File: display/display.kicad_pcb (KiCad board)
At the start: 2 copper layers, 80 x 20 mm, 48 parts, among them P1 CONN_14

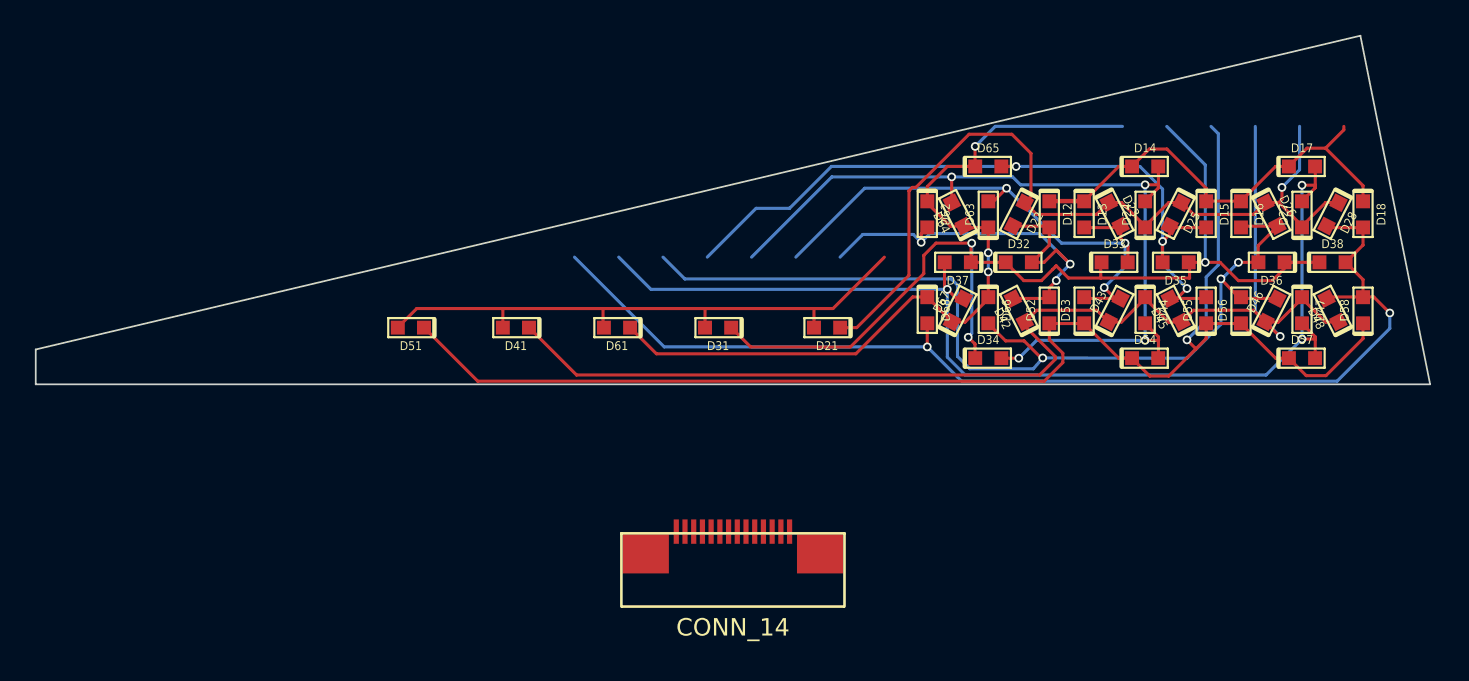
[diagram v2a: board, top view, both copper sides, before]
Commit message: Remove board contours.
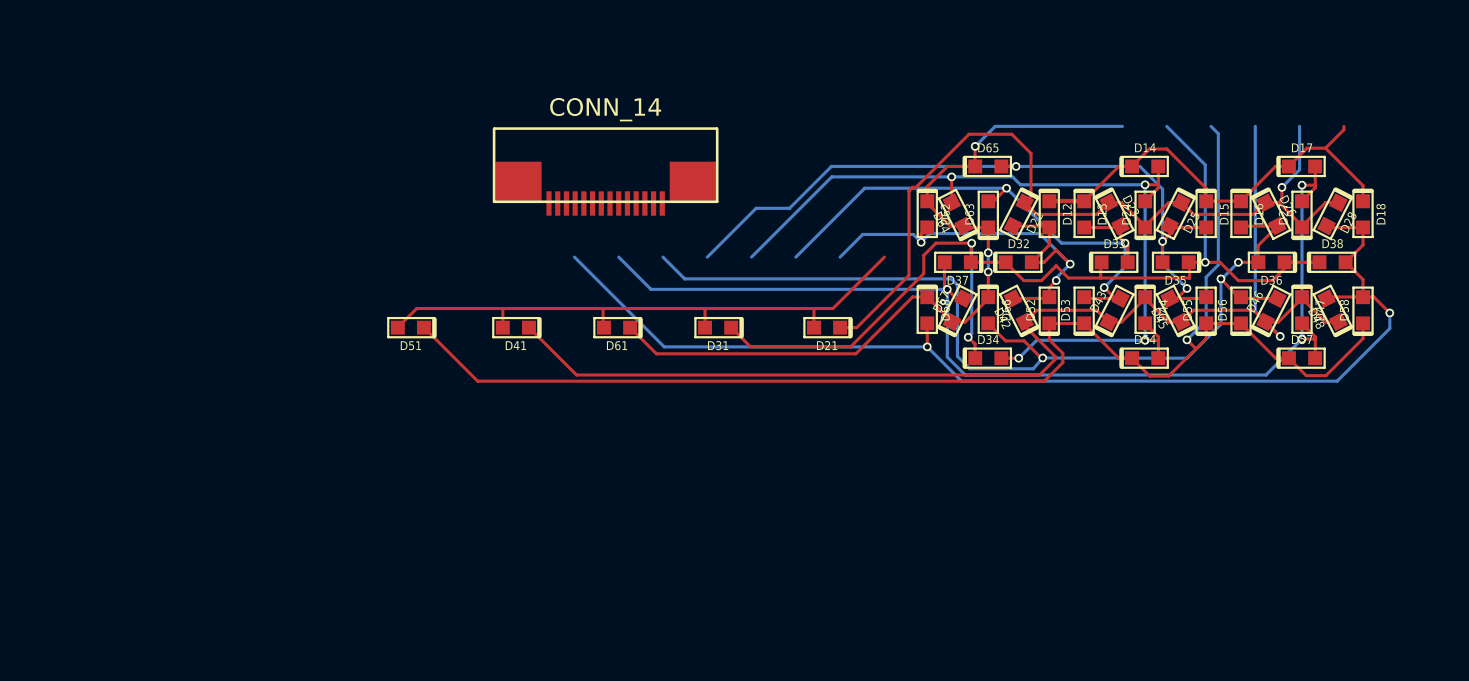
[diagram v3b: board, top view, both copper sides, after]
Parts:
- moved P1 28.4 mm to (135.4, 94.4), turned to 180 degrees
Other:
- board outline removed
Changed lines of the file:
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@@
     (area 102.642669 89.033349 182.741571 109.132371)
     (thickness 1.6002)
-    (drawings 5)
+    (drawings 1)
     (tracks 356)
     (zones 0)
@@
   )
   (module SFV14R-2STE1HLF (layer Front)
-    (at 142.69212 121.832371)
-    (fp_text reference P1 (at 0 -6.3) (layer F.SilkS) hide
+    (at 135.39 94.41 180)
+    (fp_text reference P1 (at 0 -6.3 180) (layer F.SilkS) hide
       (effects (font (size 1 1) (thickness 0.15)))
     )
-    (fp_text value CONN_14 (at 0 1.2) (layer F.SilkS)
+    (fp_text value CONN_14 (at 0 1.2 180) (layer F.SilkS)
       (effects (font (size 1 1) (thickness 0.15)))
     )
@@
     (fp_line (start -6.4 -4.2) (end 6.4 -4.2) (layer F.SilkS) (width 0.15))
     (fp_line (start -6.35 0) (end 6.35 0) (layer F.SilkS) (width 0.15))
-    (pad 4 smd rect (at -1.75 -4.3) (size 0.3 1.4)
+    (pad 4 smd rect (at -1.75 -4.3 180) (size 0.3 1.4)
       (layers Front F.Paste F.Mask)
       (net 12 /ROW4)
     )
-    (pad 5 smd rect (at -1.25 -4.3) (size 0.3 1.4)
+    (pad 5 smd rect (at -1.25 -4.3 180) (size 0.3 1.4)
       (layers Front F.Paste F.Mask)
       (net 13 /ROW5)
     )
-    (pad 6 smd rect (at -0.75 -4.3) (size 0.3 1.4)
+    (pad 6 smd rect (at -0.75 -4.3 180) (size 0.3 1.4)
       (layers Front F.Paste F.Mask)
       (net 14 /ROW6)
     )
-    (pad 7 smd rect (at -0.25 -4.3) (size 0.3 1.4)
+    (pad 7 smd rect (at -0.25 -4.3 180) (size 0.3 1.4)
       (layers Front F.Paste F.Mask)
       (net 1 /COL1)
     )
-    (pad 8 smd rect (at 0.25 -4.3) (size 0.3 1.4)
+    (pad 8 smd rect (at 0.25 -4.3 180) (size 0.3 1.4)
       (layers Front F.Paste F.Mask)
       (net 2 /COL2)
     )
-    (pad 9 smd rect (at 0.75 -4.3) (size 0.3 1.4)
+    (pad 9 smd rect (at 0.75 -4.3 180) (size 0.3 1.4)
       (layers Front F.Paste F.Mask)
       (net 3 /COL3)
     )
-    (pad 10 smd rect (at 1.25 -4.3) (size 0.3 1.4)
+    (pad 10 smd rect (at 1.25 -4.3 180) (size 0.3 1.4)
       (layers Front F.Paste F.Mask)
       (net 4 /COL4)
     )
-    (pad 11 smd rect (at 1.75 -4.3) (size 0.3 1.4)
+    (pad 11 smd rect (at 1.75 -4.3 180) (size 0.3 1.4)
       (layers Front F.Paste F.Mask)
       (net 5 /COL5)
     )
-    (pad 12 smd rect (at 2.25 -4.3) (size 0.3 1.4)
+    (pad 12 smd rect (at 2.25 -4.3 180) (size 0.3 1.4)
       (layers Front F.Paste F.Mask)
       (net 6 /COL6)
     )
-    (pad 3 smd rect (at -2.25 -4.3) (size 0.3 1.4)
+    (pad 3 smd rect (at -2.25 -4.3 180) (size 0.3 1.4)
       (layers Front F.Paste F.Mask)
       (net 11 /ROW3)
     )
-    (pad 13 smd rect (at 2.75 -4.3) (size 0.3 1.4)
+    (pad 13 smd rect (at 2.75 -4.3 180) (size 0.3 1.4)
       (layers Front F.Paste F.Mask)
       (net 7 /COL7)
     )
-    (pad 14 smd rect (at 3.25 -4.3) (size 0.3 1.4)
+    (pad 14 smd rect (at 3.25 -4.3 180) (size 0.3 1.4)
       (layers Front F.Paste F.Mask)
       (net 8 /COL8)
     )
-    (pad 2 smd rect (at -2.75 -4.3) (size 0.3 1.4)
+    (pad 2 smd rect (at -2.75 -4.3 180) (size 0.3 1.4)
       (layers Front F.Paste F.Mask)
       (net 10 /ROW2)
     )
-    (pad 1 smd rect (at -3.25 -4.3) (size 0.3 1.4)
+    (pad 1 smd rect (at -3.25 -4.3 180) (size 0.3 1.4)
       (layers Front F.Paste F.Mask)
       (net 9 /ROW1)
     )
-    (pad "" smd rect (at -5 -3.05) (size 2.65 2.3)
-      (layers Front F.Paste F.Mask)
-    )
-    (pad "" smd rect (at 5 -3.05) (size 2.65 2.3)
+    (pad "" smd rect (at -5 -3.05 180) (size 2.65 2.3)
+      (layers Front F.Paste F.Mask)
+    )
+    (pad "" smd rect (at 5 -3.05 180) (size 2.65 2.3)
       (layers Front F.Paste F.Mask)
     )
@@
     (effects (font (size 1.5 1.5) (thickness 0.3)) (justify left))
   )
-  (gr_line (start 102.6922 107.08386) (end 102.6922 109.08284) (angle 90) (layer Edge.Cuts) (width 0.09906))
-  (gr_line (start 178.69154 89.08288) (end 102.6922 107.08386) (angle 90) (layer Edge.Cuts) (width 0.09906))
-  (gr_line (start 182.69204 109.08284) (end 178.69154 89.08288) (angle 90) (layer Edge.Cuts) (width 0.09906))
-  (gr_line (start 102.6922 109.08284) (end 182.69204 109.08284) (angle 90) (layer Edge.Cuts) (width 0.09906))
   (segment (start 147.33016 105.83164) (end 147.34286 105.81894) (width 0.1778) (layer Front) (net 0))
   (segment (start 147.34286 105.81894) (end 147.34286 104.73436) (width 0.1778) (layer Front) (net 0))

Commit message: Precision-place the new contour.
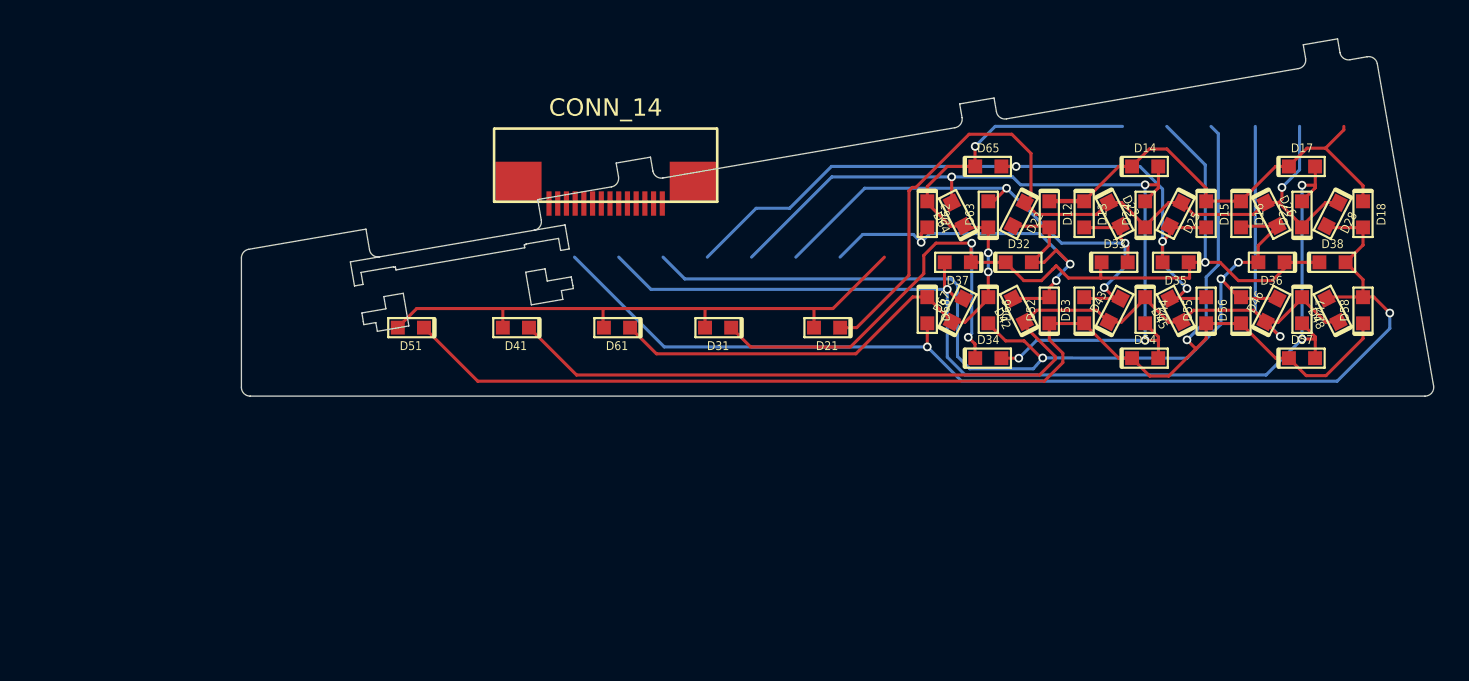
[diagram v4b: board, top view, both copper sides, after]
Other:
- board outline added: 68.4 x 20.5 mm
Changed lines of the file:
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@@
     (links 0)
     (no_connects 0)
-    (area 102.642669 89.033349 182.741571 109.132371)
+    (area 102.35 82.69 182.89528 109.763421)
     (thickness 1.6002)
-    (drawings 1)
+    (drawings 70)
     (tracks 356)
     (zones 0)
@@
     (effects (font (size 1.5 1.5) (thickness 0.3)) (justify left))
   )
+  (gr_line (start 120.742674 102.058041) (end 122.41886 101.769482) (angle 90) (layer Edge.Cuts) (width 0.01))
+  (gr_line (start 123.330283 102.353314) (end 123.231734 102.370282) (angle 90) (layer Edge.Cuts) (width 0.01))
+  (gr_line (start 123.35913 102.520856) (end 123.330283 102.353314) (angle 90) (layer Edge.Cuts) (width 0.01))
+  (gr_line (start 130.750395 101.248418) (end 123.35913 102.520856) (angle 90) (layer Edge.Cuts) (width 0.01))
+  (gr_line (start 130.721556 101.080884) (end 130.750395 101.248418) (angle 90) (layer Edge.Cuts) (width 0.01))
+  (gr_line (start 130.820105 101.063924) (end 130.721556 101.080884) (angle 90) (layer Edge.Cuts) (width 0.01))
+  (gr_line (start 130.815016 101.034352) (end 130.820105 101.063924) (angle 90) (layer Edge.Cuts) (width 0.01))
+  (gr_line (start 132.687476 100.712002) (end 130.815016 101.034352) (angle 90) (layer Edge.Cuts) (width 0.01))
+  (gr_line (start 132.806235 101.40186) (end 132.687476 100.712002) (angle 90) (layer Edge.Cuts) (width 0.01))
+  (gr_line (start 133.298987 101.317029) (end 132.806235 101.40186) (angle 90) (layer Edge.Cuts) (width 0.01))
+  (gr_line (start 133.061461 99.937321) (end 133.298987 101.317029) (angle 90) (layer Edge.Cuts) (width 0.01))
+  (gr_line (start 131.28839 100.242566) (end 133.061461 99.937321) (angle 90) (layer Edge.Cuts) (width 0.01))
+  (gr_line (start 120.9802 103.437749) (end 120.742674 102.058041) (angle 90) (layer Edge.Cuts) (width 0.01))
+  (gr_line (start 121.472945 103.352917) (end 120.9802 103.437749) (angle 90) (layer Edge.Cuts) (width 0.01))
+  (gr_line (start 121.354186 102.663068) (end 121.472945 103.352917) (angle 90) (layer Edge.Cuts) (width 0.01))
+  (gr_line (start 123.226645 102.340718) (end 121.354186 102.663068) (angle 90) (layer Edge.Cuts) (width 0.01))
+  (gr_line (start 123.231734 102.370282) (end 123.226645 102.340718) (angle 90) (layer Edge.Cuts) (width 0.01))
+  (gr_line (start 122.41886 101.769482) (end 131.28839 100.242566) (angle 90) (layer Edge.Cuts) (width 0.01))
+  (gr_line (start 130.803343 102.649754) (end 131.916968 102.458043) (angle 90) (layer Edge.Cuts) (width 0.01))
+  (gr_line (start 131.125693 104.522206) (end 130.803343 102.649754) (angle 90) (layer Edge.Cuts) (width 0.01))
+  (gr_line (start 132.934653 104.210789) (end 131.125693 104.522206) (angle 90) (layer Edge.Cuts) (width 0.01))
+  (gr_line (start 132.848128 103.708188) (end 132.934653 104.210789) (angle 90) (layer Edge.Cuts) (width 0.01))
+  (gr_line (start 133.537978 103.589421) (end 132.848128 103.708188) (angle 90) (layer Edge.Cuts) (width 0.01))
+  (gr_line (start 133.507437 103.412038) (end 133.537978 103.589421) (angle 90) (layer Edge.Cuts) (width 0.01))
+  (gr_line (start 133.447661 103.097615) (end 133.507437 103.412038) (angle 90) (layer Edge.Cuts) (width 0.01))
+  (gr_line (start 133.417128 102.920224) (end 133.447661 103.097615) (angle 90) (layer Edge.Cuts) (width 0.01))
+  (gr_line (start 132.037421 103.15775) (end 133.417128 102.920224) (angle 90) (layer Edge.Cuts) (width 0.01))
+  (gr_line (start 131.916968 102.458043) (end 132.037421 103.15775) (angle 90) (layer Edge.Cuts) (width 0.01))
+  (gr_line (start 123.777831 103.859219) (end 124.10018 105.731679) (angle 90) (layer Edge.Cuts) (width 0.01))
+  (gr_line (start 122.664206 104.050931) (end 123.777831 103.859219) (angle 90) (layer Edge.Cuts) (width 0.01))
+  (gr_line (start 122.784667 104.750638) (end 122.664206 104.050931) (angle 90) (layer Edge.Cuts) (width 0.01))
+  (gr_line (start 121.404959 104.988164) (end 122.784667 104.750638) (angle 90) (layer Edge.Cuts) (width 0.01))
+  (gr_line (start 121.4355 105.165555) (end 121.404959 104.988164) (angle 90) (layer Edge.Cuts) (width 0.01))
+  (gr_line (start 121.484305 105.481854) (end 121.4355 105.165555) (angle 90) (layer Edge.Cuts) (width 0.01))
+  (gr_line (start 121.514845 105.659245) (end 121.484305 105.481854) (angle 90) (layer Edge.Cuts) (width 0.01))
+  (gr_line (start 122.204695 105.540486) (end 121.514845 105.659245) (angle 90) (layer Edge.Cuts) (width 0.01))
+  (gr_line (start 122.29122 106.043095) (end 122.204695 105.540486) (angle 90) (layer Edge.Cuts) (width 0.01))
+  (gr_line (start 124.10018 105.731679) (end 122.29122 106.043095) (angle 90) (layer Edge.Cuts) (width 0.01))
+  (gr_arc (start 122.334027 101.276742) (end 121.841277 101.361561) (angle -90.01309679) (layer Edge.Cuts) (width 0.01))
+  (gr_arc (start 131.203563 99.749815) (end 131.28839 100.242566) (angle -90.00377062) (layer Edge.Cuts) (width 0.01))
+  (gr_line (start 121.841277 101.361561) (end 121.637694 100.17896) (angle 90) (layer Edge.Cuts) (width 0.01))
+  (gr_line (start 131.49272 98.482381) (end 131.696311 99.664983) (angle 90) (layer Edge.Cuts) (width 0.01))
+  (gr_line (start 114.907893 101.337514) (end 121.637694 100.17896) (angle 90) (layer Edge.Cuts) (width 0.01))
+  (gr_line (start 114.49272 109.25842) (end 114.49272 101.830266) (angle 90) (layer Edge.Cuts) (width 0.01))
+  (gr_line (start 182.397742 109.75842) (end 114.99272 109.75842) (angle 90) (layer Edge.Cuts) (width 0.01))
+  (gr_line (start 179.660719 90.696156) (end 182.890273 109.172322) (angle 90) (layer Edge.Cuts) (width 0.01))
+  (gr_line (start 178.096594 90.45937) (end 179.083357 90.289494) (angle 90) (layer Edge.Cuts) (width 0.01))
+  (gr_line (start 158.386534 93.852521) (end 175.140082 90.968343) (angle 90) (layer Edge.Cuts) (width 0.01))
+  (gr_line (start 138.676474 97.245679) (end 155.430022 94.361493) (angle 90) (layer Edge.Cuts) (width 0.01))
+  (gr_line (start 131.49272 98.482381) (end 135.719962 97.754651) (angle 90) (layer Edge.Cuts) (width 0.01))
+  (gr_arc (start 114.99272 101.830261) (end 114.907893 101.337514) (angle -80.22798794) (layer Edge.Cuts) (width 0.01))
+  (gr_arc (start 114.992716 109.25842) (end 114.49272 109.25842) (angle -89.99818777) (layer Edge.Cuts) (width 0.01))
+  (gr_arc (start 182.397723 109.258422) (end 182.397742 109.75842) (angle -99.89535664) (layer Edge.Cuts) (width 0.01))
+  (gr_arc (start 179.168185 90.782243) (end 179.660719 90.696156) (angle -89.85795299) (layer Edge.Cuts) (width 0.01))
+  (gr_arc (start 178.011762 89.966623) (end 177.519011 90.051449) (angle -90.00377062) (layer Edge.Cuts) (width 0.01))
+  (gr_arc (start 175.055252 90.475593) (end 175.140082 90.968343) (angle -89.98998598) (layer Edge.Cuts) (width 0.01))
+  (gr_line (start 177.519011 90.051449) (end 177.383284 89.263043) (angle 90) (layer Edge.Cuts) (width 0.01))
+  (gr_line (start 177.383284 89.263043) (end 175.412284 89.60236) (angle 90) (layer Edge.Cuts) (width 0.01))
+  (gr_line (start 175.412284 89.60236) (end 175.54801 90.390767) (angle 90) (layer Edge.Cuts) (width 0.01))
+  (gr_arc (start 158.301702 93.359781) (end 157.808951 93.4446) (angle -90.01309679) (layer Edge.Cuts) (width 0.01))
+  (gr_line (start 157.808951 93.4446) (end 157.673224 92.656201) (angle 90) (layer Edge.Cuts) (width 0.01))
+  (gr_line (start 157.673224 92.656201) (end 155.702223 92.995511) (angle 90) (layer Edge.Cuts) (width 0.01))
+  (gr_line (start 155.702223 92.995511) (end 155.837943 93.783917) (angle 90) (layer Edge.Cuts) (width 0.01))
+  (gr_arc (start 155.345182 93.86874) (end 155.430022 94.361493) (angle -89.98999186) (layer Edge.Cuts) (width 0.01))
+  (gr_arc (start 138.591645 96.752926) (end 138.098891 96.83775) (angle -90.00032678) (layer Edge.Cuts) (width 0.01))
+  (gr_line (start 138.098891 96.83775) (end 137.963164 96.049351) (angle 90) (layer Edge.Cuts) (width 0.01))
+  (gr_line (start 137.963164 96.049351) (end 135.992156 96.388669) (angle 90) (layer Edge.Cuts) (width 0.01))
+  (gr_line (start 135.992156 96.388669) (end 136.127883 97.177067) (angle 90) (layer Edge.Cuts) (width 0.01))
+  (gr_arc (start 135.635143 97.2619) (end 135.719962 97.754651) (angle -90.01309679) (layer Edge.Cuts) (width 0.01))
   (segment (start 147.33016 105.83164) (end 147.34286 105.81894) (width 0.1778) (layer Front) (net 0))
   (segment (start 147.34286 105.81894) (end 147.34286 104.73436) (width 0.1778) (layer Front) (net 0))

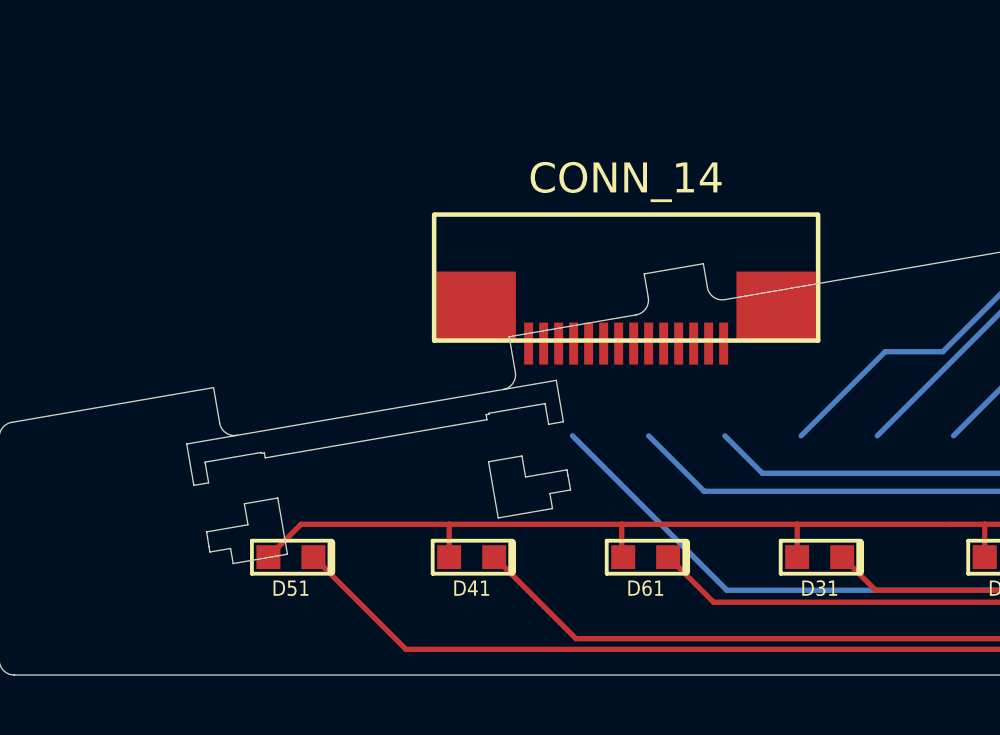
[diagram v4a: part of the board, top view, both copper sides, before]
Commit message: Place the connector along its contour.
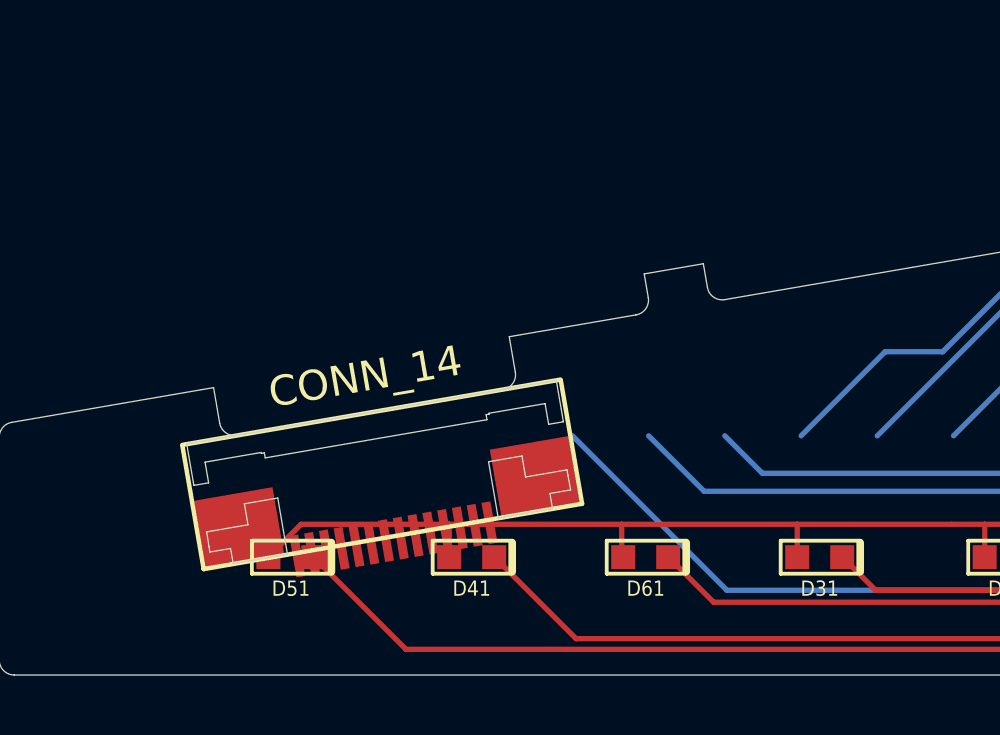
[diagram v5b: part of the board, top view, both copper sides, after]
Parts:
- moved P1 10.7 mm to (126.9, 101.0), turned to 189.8 degrees
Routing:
- net /COL7: track 0.00 -> 78.8 mm, vias 0 -> 1
- net (no net): track 699.0 -> 620.2 mm, vias 30 -> 29
